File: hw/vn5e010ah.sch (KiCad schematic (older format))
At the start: 3 parts, among them U1001 VN5E010AH

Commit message: 3.0.0 hw with low side heater mosfet
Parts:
- R1001: symbol 390 -> fsb-rescue:390
- R502: symbol 1K -> fsb-rescue:1K
- U1001: symbol VN5E010AH -> fsb-rescue:VN5E010AH
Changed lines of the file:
@@
-EESchema Schematic File Version 2
-LIBS:fsb-rescue
-LIBS:kemet
-LIBS:power
-LIBS:usevolt
-LIBS:wurth_elektronik_LED
-LIBS:yageo
+EESchema Schematic File Version 4
 LIBS:fsb-cache
 EELAYER 26 0
@@
 	4350 3450 4600 3450
 $Comp
-L VDD #PWR602
+L fsb-rescue:VDD #PWR602
 U 1 1 59D7E637
 P 4600 3000
@@
 AR Path="/5A13680F/59D7E637" Ref="#PWR1202"  Part="1"
 AR Path="/5A14370A/59D7E637" Ref="#PWR1302"  Part="1"
-AR Path="/5A33548E/59D7E637" Ref="#PWR602"  Part="1"
+AR Path="/5A33548E/59D7E637" Ref="#PWR0602"  Part="1"
 AR Path="/5A33648A/59D7E637" Ref="#PWR031"  Part="1"
-F 0 "#PWR602" H 4600 2850 50  0001 C CNN
+F 0 "#PWR0602" H 4600 2850 50  0001 C CNN
 F 1 "VDD" H 4617 3173 50  0000 C CNN
 F 2 "" H 4600 3000 50  0000 C CNN
@@
 Connection ~ 4600 3300
 $Comp
-L GND #PWR601
+L fsb-rescue:GND #PWR601
 U 1 1 5A014ACD
 P 3850 3600
@@
 AR Path="/5A13680F/5A014ACD" Ref="#PWR1201"  Part="1"
 AR Path="/5A14370A/5A014ACD" Ref="#PWR1301"  Part="1"
-AR Path="/5A33548E/5A014ACD" Ref="#PWR601"  Part="1"
+AR Path="/5A33548E/5A014ACD" Ref="#PWR0601"  Part="1"
 AR Path="/5A33648A/5A014ACD" Ref="#PWR032"  Part="1"
-F 0 "#PWR601" H 3850 3350 50  0001 C CNN
+F 0 "#PWR0601" H 3850 3350 50  0001 C CNN
 F 1 "GND" H 3855 3427 50  0000 C CNN
 F 2 "" H 3850 3600 50  0000 C CNN
@@
 	3850 3300 3850 3600
 $Comp
-L 1K R502
+L fsb-rescue:1K R502
 U 1 1 5A058D94
 P 3600 3350
@@
 Connection ~ 3850 3550
 $Comp
-L 390 R1001
+L fsb-rescue:390 R1001
 U 1 1 5A32CF0E
 P 4150 3300
@@
 $EndComp
 $Comp
-L VN5E010AH U1001
+L fsb-rescue:VN5E010AH U1001
 U 1 1 5A32CF4A
 P 5300 3300
@@
 $EndComp
 $Comp
-L GND #PWR1003
+L fsb-rescue:GND #PWR1003
 U 1 1 5A32CF90
 P 4800 3600
@@
 AR Path="/5A1358B0/5A32CF90" Ref="#PWR1103"  Part="1"
 AR Path="/5A13680F/5A32CF90" Ref="#PWR1203"  Part="1"
-AR Path="/5A33548E/5A32CF90" Ref="#PWR603"  Part="1"
+AR Path="/5A33548E/5A32CF90" Ref="#PWR0603"  Part="1"
 AR Path="/5A33648A/5A32CF90" Ref="#PWR033"  Part="1"
-F 0 "#PWR603" H 4800 3350 50  0001 C CNN
+F 0 "#PWR0603" H 4800 3350 50  0001 C CNN
 F 1 "GND" H 4805 3427 50  0000 C CNN
 F 2 "" H 4800 3600 50  0000 C CNN

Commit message: HAL updated to latest uv bootloader, starting to draw 6.0.0 pcb
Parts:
- removed R1001: 390, yageo:0603, symbol fsb-rescue:390
- added D3: ZENER_MM3Z3V6T1G, usevolt:SOD-323, symbol usevolt:ZENER_MM3Z3V6T1G
- added R1: 10K, yageo:0603, symbol yageo:10K
- added R709: 1K, yageo:0603, symbol yageo:1K
- R502: symbol fsb-rescue:1K -> yageo:1K
- U1001: symbol fsb-rescue:VN5E010AH -> usevolt:VN5E010AH
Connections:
- net GND: now also D3.2, R1.1 (R1), R709.1 (R1)
- net OUT1: now also R1.2 (R2)
- net SENSE1: now also D3.1, R709.2 (R2)

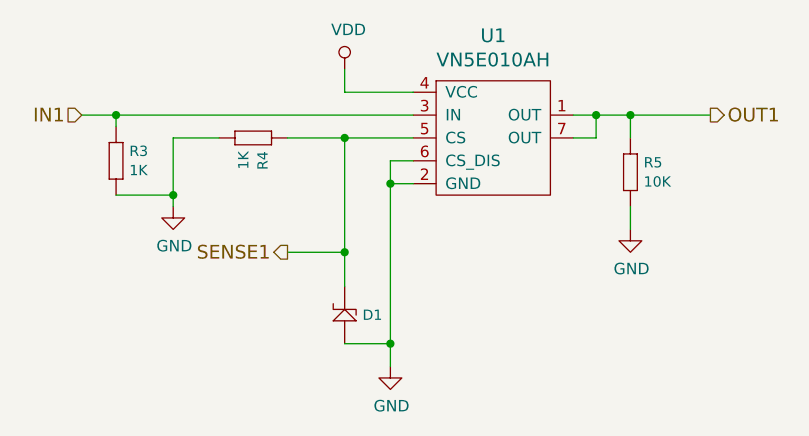
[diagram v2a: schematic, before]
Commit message: hw 6.0.0 created, fits uw aluminium enclosure
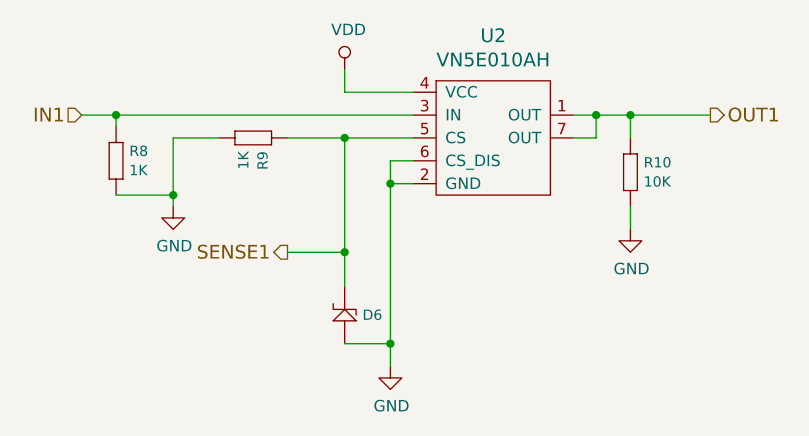
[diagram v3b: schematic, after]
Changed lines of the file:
@@
 $Descr A4 11693 8268
 encoding utf-8
-Sheet 6 8
+Sheet 9 8
 Title ""
 Date ""
@@
 AR Path="/5A14370A/59D7E637" Ref="#PWR051"  Part="1"
 AR Path="/5A33548E/59D7E637" Ref="#PWR0111"  Part="1"
-F 0 "#PWR0111" H 4600 2850 50  0001 C CNN
+AR Path="/5C4B29BE/59D7E637" Ref="#PWR02"  Part="1"
+AR Path="/5C4B2C63/59D7E637" Ref="#PWR06"  Part="1"
+F 0 "#PWR02" H 4600 2850 50  0001 C CNN
 F 1 "VDD" H 4617 3173 50  0000 C CNN
 F 2 "" H 4600 3000 50  0000 C CNN
@@
 AR Path="/5A14370A/5A014ACD" Ref="#PWR052"  Part="1"
 AR Path="/5A33548E/5A014ACD" Ref="#PWR0112"  Part="1"
-F 0 "#PWR0112" H 3850 3350 50  0001 C CNN
+AR Path="/5C4B29BE/5A014ACD" Ref="#PWR01"  Part="1"
+AR Path="/5C4B2C63/5A014ACD" Ref="#PWR05"  Part="1"
+F 0 "#PWR01" H 3850 3350 50  0001 C CNN
 F 1 "GND" H 3855 3427 50  0000 C CNN
 F 2 "" H 3850 3600 50  0000 C CNN
@@
 AR Path="/5A14370A/5A058D94" Ref="R1602"  Part="1"
 AR Path="/5A33548E/5A058D94" Ref="R3"  Part="1"
-F 0 "R3" V 3608 3408 45  0000 L CNN
+AR Path="/5C4B29BE/5A058D94" Ref="R8"  Part="1"
+AR Path="/5C4B2C63/5A058D94" Ref="R11"  Part="1"
+F 0 "R8" V 3608 3408 45  0000 L CNN
 F 1 "1K" V 3692 3408 45  0000 L CNN
 F 2 "yageo:0603" H 3630 3500 20  0001 C CNN
@@
 AR Path="/5A13680F/5A32CF4A" Ref="U1201"  Part="1"
 AR Path="/5A33548E/5A32CF4A" Ref="U1"  Part="1"
-F 0 "U1" H 5250 3747 60  0000 C CNN
+AR Path="/5C4B29BE/5A32CF4A" Ref="U2"  Part="1"
+AR Path="/5C4B2C63/5A32CF4A" Ref="U3"  Part="1"
+F 0 "U2" H 5250 3747 60  0000 C CNN
 F 1 "VN5E010AH" H 5250 3641 60  0000 C CNN
 F 2 "usevolt:HPAK" H 4950 4250 60  0001 C CNN
@@
 AR Path="/5A13680F/5A32CF90" Ref="#PWR050"  Part="1"
 AR Path="/5A33548E/5A32CF90" Ref="#PWR0113"  Part="1"
-F 0 "#PWR0113" H 4800 4050 50  0001 C CNN
+AR Path="/5C4B29BE/5A32CF90" Ref="#PWR03"  Part="1"
+AR Path="/5C4B2C63/5A32CF90" Ref="#PWR07"  Part="1"
+F 0 "#PWR03" H 4800 4050 50  0001 C CNN
 F 1 "GND" H 4805 4127 50  0000 C CNN
 F 2 "" H 4800 4300 50  0000 C CNN
@@
 AR Path="/5A14370A/5B23824A" Ref="R1202"  Part="1"
 AR Path="/5A33548E/5B23824A" Ref="R4"  Part="1"
-F 0 "R4" V 4258 3358 45  0000 L CNN
+AR Path="/5C4B29BE/5B23824A" Ref="R9"  Part="1"
+AR Path="/5C4B2C63/5B23824A" Ref="R12"  Part="1"
+F 0 "R9" V 4258 3358 45  0000 L CNN
 F 1 "1K" V 4342 3358 45  0000 L CNN
 F 2 "yageo:0603" H 4280 3450 20  0001 C CNN
@@
 AR Path="/5A1358B0/5BA9BFAA" Ref="R4"  Part="1"
 AR Path="/5A33548E/5BA9BFAA" Ref="R5"  Part="1"
-F 0 "R5" V 5858 3458 45  0000 L CNN
+AR Path="/5C4B29BE/5BA9BFAA" Ref="R10"  Part="1"
+AR Path="/5C4B2C63/5BA9BFAA" Ref="R13"  Part="1"
+F 0 "R10" V 5858 3458 45  0000 L CNN
 F 1 "10K" V 5942 3458 45  0000 L CNN
 F 2 "yageo:0603" H 5880 3550 20  0001 C CNN
@@
 AR Path="/5A1358B0/5BA9C33E" Ref="#PWR0109"  Part="1"
 AR Path="/5A33548E/5BA9C33E" Ref="#PWR0114"  Part="1"
-F 0 "#PWR0114" H 5850 3450 50  0001 C CNN
+AR Path="/5C4B29BE/5BA9C33E" Ref="#PWR04"  Part="1"
+AR Path="/5C4B2C63/5BA9C33E" Ref="#PWR08"  Part="1"
+F 0 "#PWR04" H 5850 3450 50  0001 C CNN
 F 1 "GND" H 5855 3527 50  0000 C CNN
 F 2 "" H 5850 3700 50  0000 C CNN
@@
 AR Path="/5A1358B0/5BAABE3C" Ref="D6"  Part="1"
 AR Path="/5A33548E/5BAABE3C" Ref="D1"  Part="1"
-F 0 "D1" V 4525 3922 45  0000 R CNN
+AR Path="/5C4B29BE/5BAABE3C" Ref="D6"  Part="1"
+AR Path="/5C4B2C63/5BAABE3C" Ref="D7"  Part="1"
+F 0 "D6" V 4525 3922 45  0000 R CNN
 F 1 "ZENER_MM3Z3V6T1G" H 4875 4375 45  0001 L BNN
 F 2 "usevolt:SOD-323" H 4575 4375 20  0001 C CNN
